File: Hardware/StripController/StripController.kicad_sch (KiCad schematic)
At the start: 50 parts, among them IC1 RY8310, IC2 CH32V003F4U6, J1 Conn_01x03_Socket, J2 Conn_01x06_Socket, J4 Conn_01x02_Pin, J5 TagConnect, J6 Conn_01x03_Socket, Q1 AON7544, Q2 AON7544, Q3 AON7544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

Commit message: edit pcb desine
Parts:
- added C12, C13: 100n, Capacitor_SMD:C_0402_1005Metric, symbol Device:C
- added D5: 5,1V, symbol Device:D_Zener
- added F2: 0,2A, Fuse:Fuse_0402_1005Metric, symbol Device:Fuse
- added R14, R18: R, Resistor_SMD:R_0402_1005Metric, symbol Device:R
- added R15: 10k, Resistor_SMD:R_0402_1005Metric, symbol Device:R
- added R16, R17: 0, Resistor_SMD:R_0402_1005Metric, symbol Device:R
- added R19: 100k, Resistor_SMD:R_0402_1005Metric, symbol Device:R
- added TH1: Thermistor_NTC, Resistor_SMD:R_0402_1005Metric, symbol Device:Thermistor_NTC
- F1: value Fuse -> 10A
- Q1, Q2, Q3, Q4, Q5: footprint Package_DFN_QFN:DFN-8-1EP_3x3mm_P0.5mm_EP1.65x2.38mm_ThermalVias -> Techbeard:AON7544
- R7: value NC -> 1k; now not fitted
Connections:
- net U4_RO is gone; now on net U2_RO: IC2.20 (PD6), U4.1 (RO)
- net +5V: now also R19.1; no longer U2.2 (~{RE}), U2.3 (DE)
- net B: now also Q2.4 (G), R8.2; no longer Q4.4 (G), R9.2
- net G: now also Q4.4 (G), R9.2; no longer Q3.4 (G), R6.2
- net GND: now also C12.2, C13.2, D5.2 (A), R15.1, R18.2, TH1.2; no longer U4.2 (~{RE}), U4.3 (DE)
- net R: now also Q3.4 (G), R6.2; no longer Q2.4 (G), R8.2
- net RA: now also R17.1
- net RB: now also R16.2
- net StateLed0: now also D4.1 (K); no longer D3.1 (K)
- net StateLed1: now also D3.1 (K); no longer D4.1 (K)
- net TA: now also R17.2
- net TB: now also R16.1
- net VCC: now also R14.1; no longer Q6.3 (D)
- net at F1.1, J4.1 (Pin_1): now also F2.1
- net Voltage: now reaches IC2.10 (PC3)
- net Voltage: now also C12.1, D5.1 (K), R14.2, R18.1
- net U2_DE: now reaches IC2.11 (PC4)
- net U2_DE: now also U2.3 (DE)
- net U2_RE: now reaches IC2.12 (PC5)
- net U2_RE: now also U2.2 (~{RE})
- net Temp: now reaches IC2.16 (PD2)
- net Temp: now also C13.1, R19.2, TH1.1
- new net: F2.2, Q6.3 (D)
- new net: R15.2, U4.2 (~{RE}), U4.3 (DE)
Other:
- moved on the sheet: C10, C11, C2, C5, C8, D2, D3, D4, F1, H1, H2, H3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

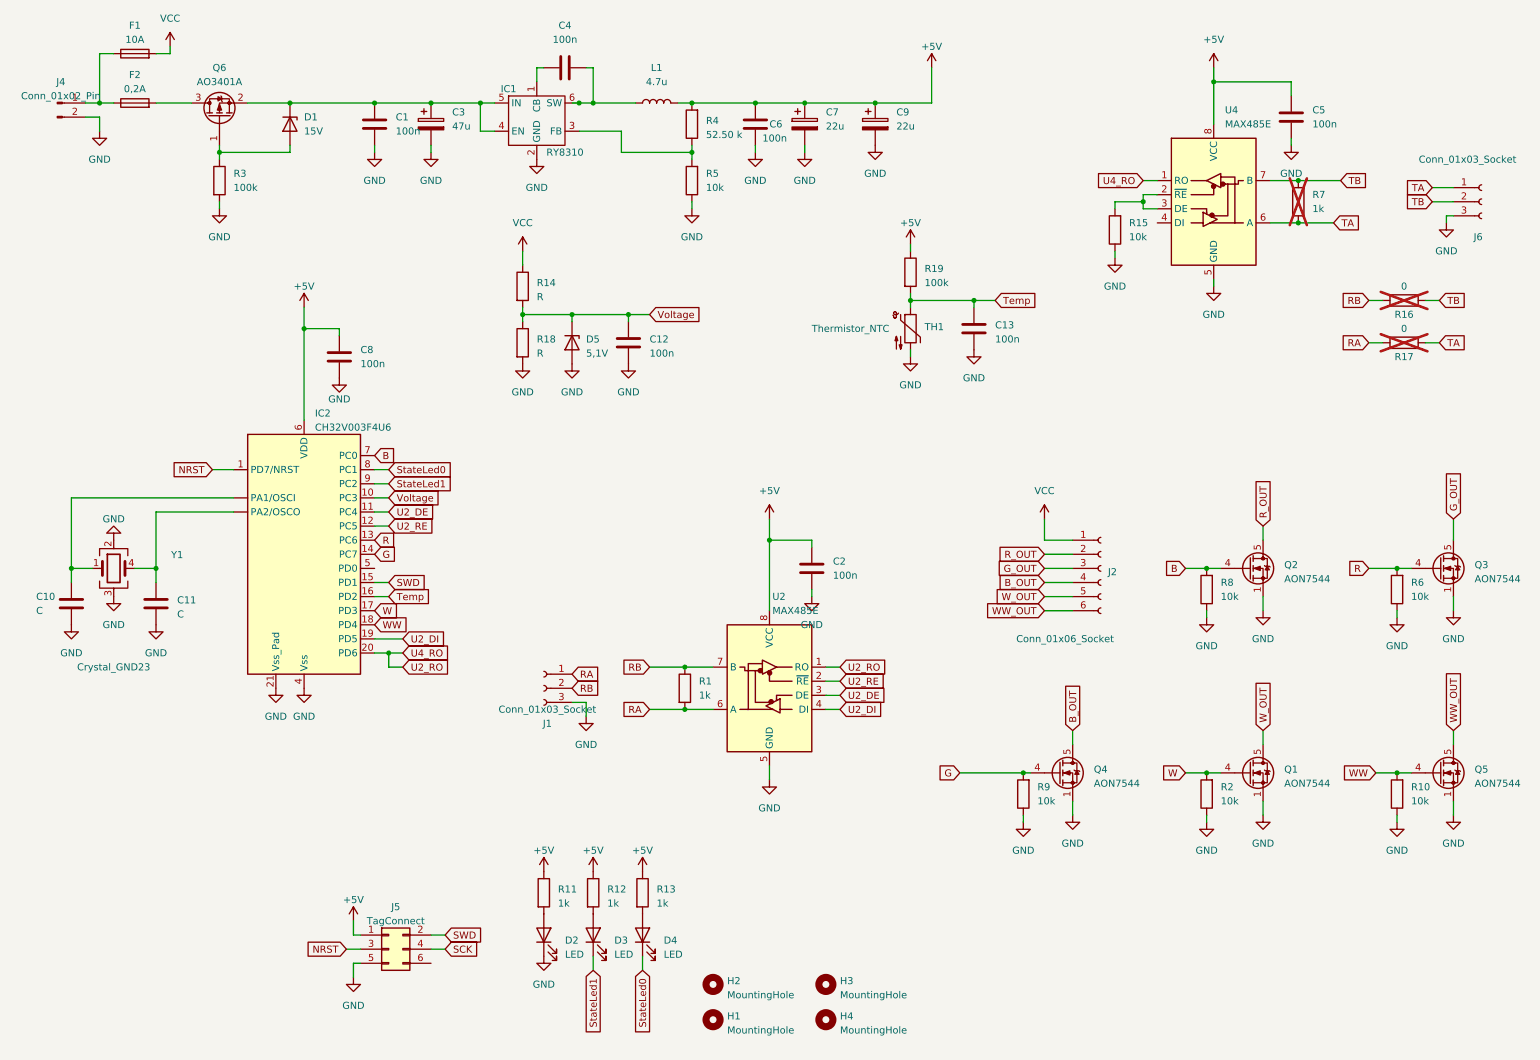
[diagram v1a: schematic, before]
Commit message: add CCController
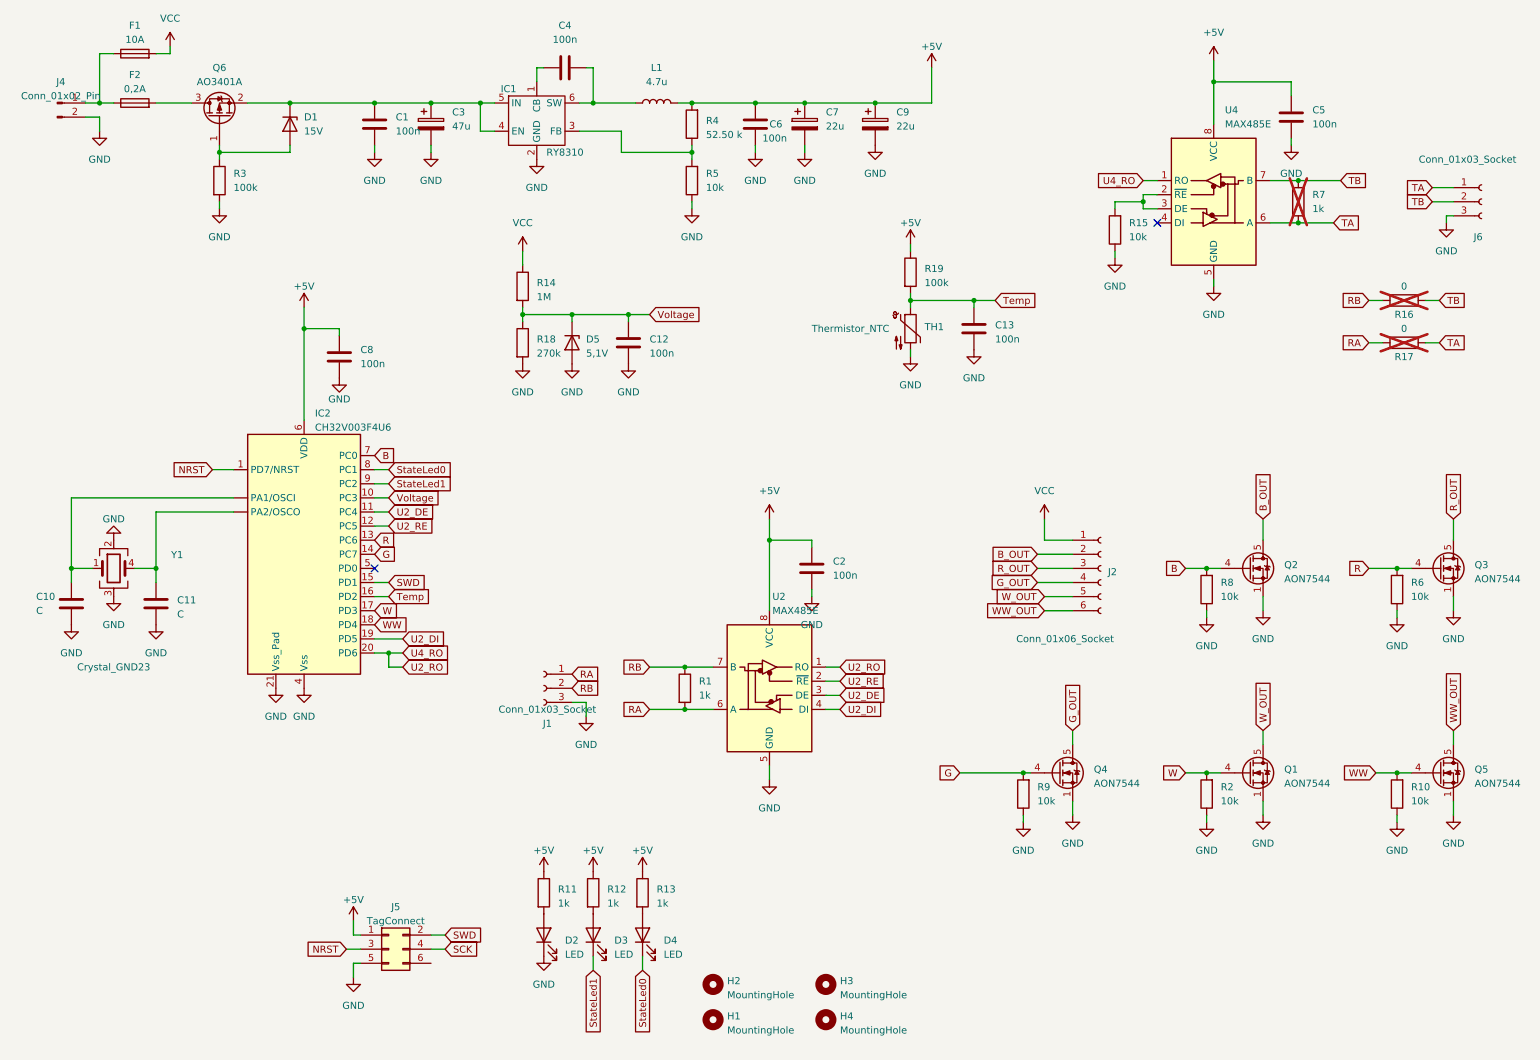
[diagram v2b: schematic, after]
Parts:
- Q1, Q2, Q3, Q4, Q5: footprint Techbeard:AON7544 -> Package_TO_SOT_SMD:TDSON-8-1
- R14: value R -> 1M
- R18: value R -> 270k
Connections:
- net B_OUT: now also J2.2 (Pin_2), Q2.5 (D); no longer J2.4 (Pin_4), Q4.5 (D)
- net G_OUT: now also J2.4 (Pin_4), Q4.5 (D); no longer J2.3 (Pin_3), Q3.5 (D)
- net R_OUT: now also J2.3 (Pin_3), Q3.5 (D); no longer J2.2 (Pin_2), Q2.5 (D)
- no-connect marks 0 -> 2

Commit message: edit Strip controller and buy first batch
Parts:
- removed F1: 10A, Fuse:Fuseholder_Clip-5x20mm_Schurter_CQM_Inline_P20.60x5.00mm_D1.00mm_Horizontal, symbol Device:Fuse
- removed Y1: Crystal_GND23, symbol Device:Crystal_GND23
- added J10, J9: F1, Techbeard:Fuseholder C3130, symbol Connector:Conn_01x01_Pin
- added J3: SWD, TestPoint:TestPoint_Pad_1.5x1.5mm, symbol Connector:Conn_01x01_Pin
- added J7: +5V, TestPoint:TestPoint_Pad_1.5x1.5mm, symbol Connector:Conn_01x01_Pin
- added J8: GND, TestPoint:TestPoint_Pad_1.5x1.5mm, symbol Connector:Conn_01x01_Pin
- added R20, R21, R22, R23, R24: 47, Resistor_SMD:R_0402_1005Metric, symbol Device:R
- added Y2: Crystal_GND24, Crystal:Crystal_SMD_3225-4Pin_3.2x2.5mm, symbol Device:Crystal_GND24
- C10, C11: now not fitted
- C3: value 47u -> 22u
- D1: footprint Diode_SMD:D_0402_1005Metric -> Diode_SMD:D_SOD-323
- D2: value LED -> PWR; footprint LED_SMD:LED_0402_1005Metric -> LED_SMD:LED_0603_1608Metric
- D3: value LED -> S1; footprint LED_SMD:LED_0402_1005Metric -> LED_SMD:LED_0603_1608Metric
- D4: value LED -> S2; footprint LED_SMD:LED_0402_1005Metric -> LED_SMD:LED_0603_1608Metric
- D5: footprint (none) -> Diode_SMD:D_SOD-323
- L1: footprint Inductor_SMD:L_Abracon_ASPI-0630LR -> Techbeard:L_0630
- Q1, Q2, Q3, Q4, Q5: footprint Package_TO_SOT_SMD:TDSON-8-1 -> Techbeard:AON7544
- Q6: footprint Package_TO_SOT_SMD:SOT-23 -> Package_TO_SOT_SMD:TSOT-23
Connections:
- net +5V: now also J7.1 (Pin_1)
- net B: now also IC2.14 (PC7), R22.1; no longer IC2.7 (PC0), Q2.4 (G), R8.2
- net B_OUT: now also J2.4 (Pin_4), Q4.5 (D); no longer J2.2 (Pin_2), Q2.5 (D)
- net G: now also IC2.13 (PC6), R21.1; no longer IC2.14 (PC7), Q4.4 (G), R9.2
- net GND: now also J8.1 (Pin_1), Y2.2, Y2.4
- net G_OUT: now also J2.3 (Pin_3), Q3.5 (D); no longer J2.4 (Pin_4), Q4.5 (D)
- net R: now also IC2.7 (PC0), R20.1; no longer IC2.13 (PC6), Q3.4 (G), R6.2
- net R_OUT: now also J2.2 (Pin_2), Q2.5 (D); no longer J2.3 (Pin_3), Q3.5 (D)
- net SWD: now also J3.1 (Pin_1)
- net VCC: now also J10.1 (Pin_1)
- net W: now also R23.1; no longer Q1.4 (G), R2.2
- net WW: now also R24.1; no longer Q5.4 (G), R10.2
- net at F2.1, J4.1 (Pin_1): now also J9.1 (Pin_1)
- net at C10.1: now also IC2.2 (PA1/OSCI), Y2.1; no longer IC2. (PA2/OSCO)
- net at C11.1: now also IC2.3 (PA2/OSCO), Y2.3; no longer IC2. (PA2/OSCO)
- new net: Q1.4 (G), R2.2, R23.2
- new net: Q4.4 (G), R22.2, R9.2
- new net: Q3.4 (G), R21.2, R6.2
- new net: Q2.4 (G), R20.2, R8.2
- new net: Q5.4 (G), R10.2, R24.2
